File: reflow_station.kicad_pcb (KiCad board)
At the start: 2 copper layers, 6.5 x 0.7 mm, 252 parts, among them IC1 AMC23C10DWVR, IC2 MP100LGN-Z, J1 1731734, J10 DG301-5.0-02P-12-00A_H_, J11 USB_A, J12 USB_C_Receptacle_USB2.0_16P, J13 Conn_ARM_JTAG_SWD_10, J2 1707027, J3 1707027, J4 F52Q-1A7H1-11015, J5 1707027, J6 1707027, J7 DG301-5.0-02P-12-00A_H_, J8 DG301-5.0-02P-12-00A_H_, J9 DG301-5.0-02P-12-00A_H_, M1 Fan_CPU_4pin, M2 Fan_CPU_4pin, M3 Fan_CPU_4pin, M4 Fan_CPU_4pin, Q1 BTA16-600B, Q2 BTA16-600B, Q3 BTA16-600B, Q4 BTA16-600B, Q5 KSC1815YTA, SW2 SW_DIP_x08, SW3 SW_SPST, SW4 SW_SPST, SW5 SW_SPST, SW6 SW_Push, SW7 SW_SPDT, SW8 SW_SPDT, U1 TPS82130, U10 TPS2051BDBVR, U11 RCLAMP0504F.TCT, U12 STM32F469VITx, U13 RCLAMP0504F.TCT, U14 RCLAMP0504F.TCT, U2 RAC20-12SK, U3 MOC3023M, U4 MOC3023M, U5 TPS82130, U6 MOC3023M, U7 MOC3023M, U8 ADS1118IDGS, U9 ADS1118IDGS, Y1 25MHz, Y2 32.768kHz

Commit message: feat: populate elements on board
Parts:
- C1: footprint reflow_station_library:C_Axial_L12.0mm_D6.5mm_P15.00mm_Horizontal -> reflow_station_library:R474N31005001K
- R3: footprint reflow_station_library:R_0805_2012Metric_Pad1.20x1.40mm_HandSolder -> reflow_station_library:R_0402_1005Metric
- moved D5 132.4 mm to (78.6, 37.2)
- moved D2 130.2 mm to (78.6, 39.0)
- moved D1 128.1 mm to (78.6, 41.0)
- moved R3 118.7 mm to (90.9, 46.2), turned to 90 degrees
- moved C10 108.7 mm to (118.2, 129.3), turned to 90 degrees
- moved C15 108.3 mm to (97.0, 41.8)
- moved R27 104.5 mm to (81.5, 37.3)
- moved C11 103.7 mm to (116.2, 129.3)
- moved J1 101.6 mm to (79.1, 128.4)
- moved C16 100.2 mm to (111.8, 120.5), turned to 90 degrees
- moved C6 100.2 mm to (117.6, 114.9), turned to 180 degrees
- moved C20 99.2 mm to (115.1, 119.9), turned to -90 degrees
- moved R32 97.5 mm to (100.0, 39.9), turned to -90 degrees
- moved R31 97.5 mm to (100.0, 37.9), turned to -90 degrees
- moved R2 97.3 mm to (81.3, 39.1)
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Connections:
- D4 pad 2: /N -> GND1
- D4 pad 4: GND1 -> /N
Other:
- board size 6.5 x 0.7 mm -> 150 x 100 mm
- copper layers 2 -> 6

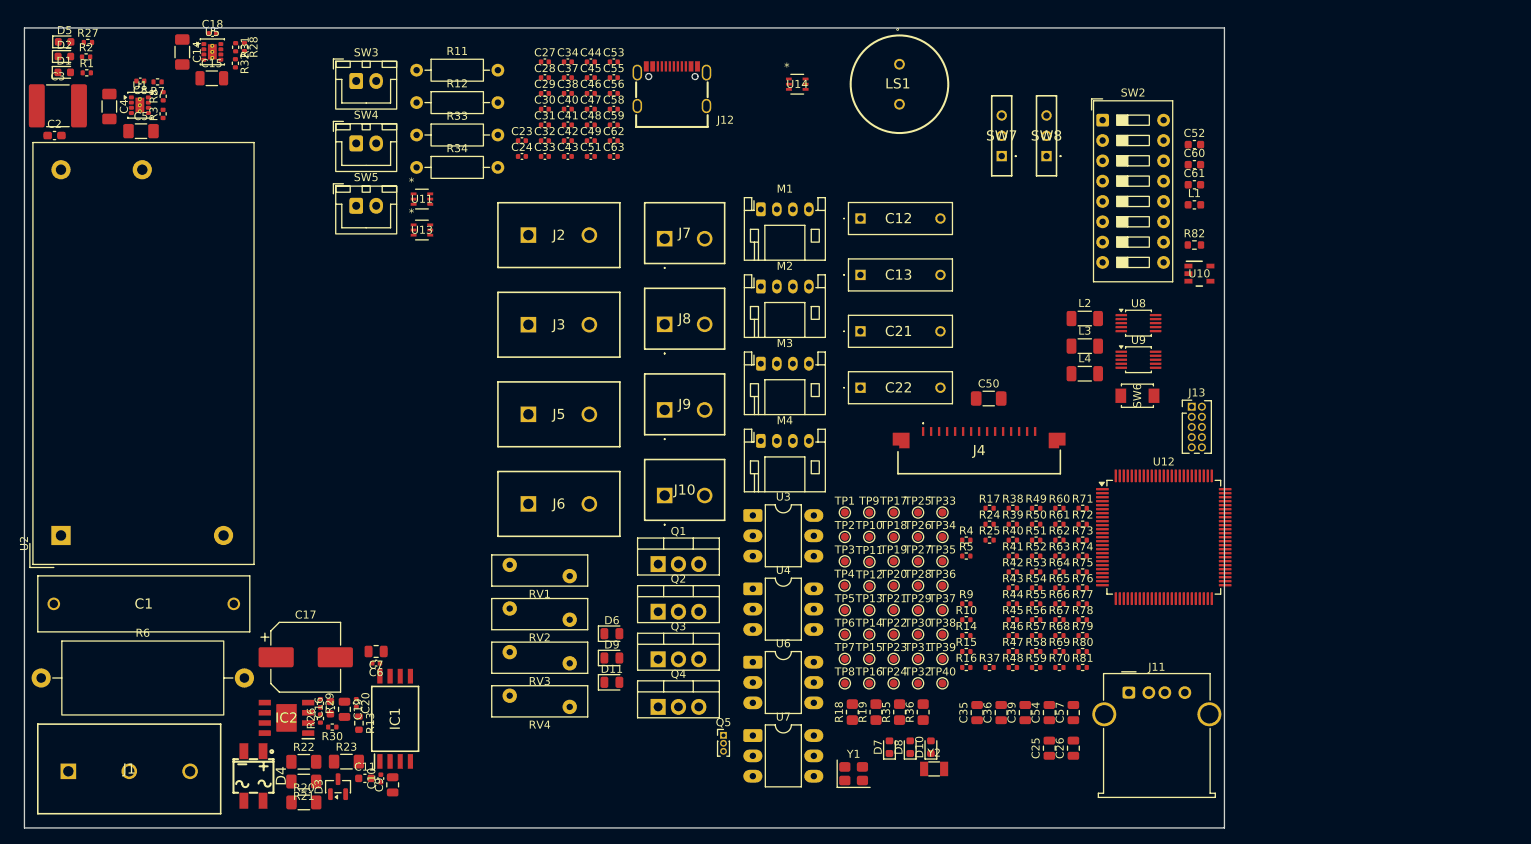
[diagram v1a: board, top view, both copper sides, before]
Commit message: feat: resize board; position elements more accurately; add mounting holes
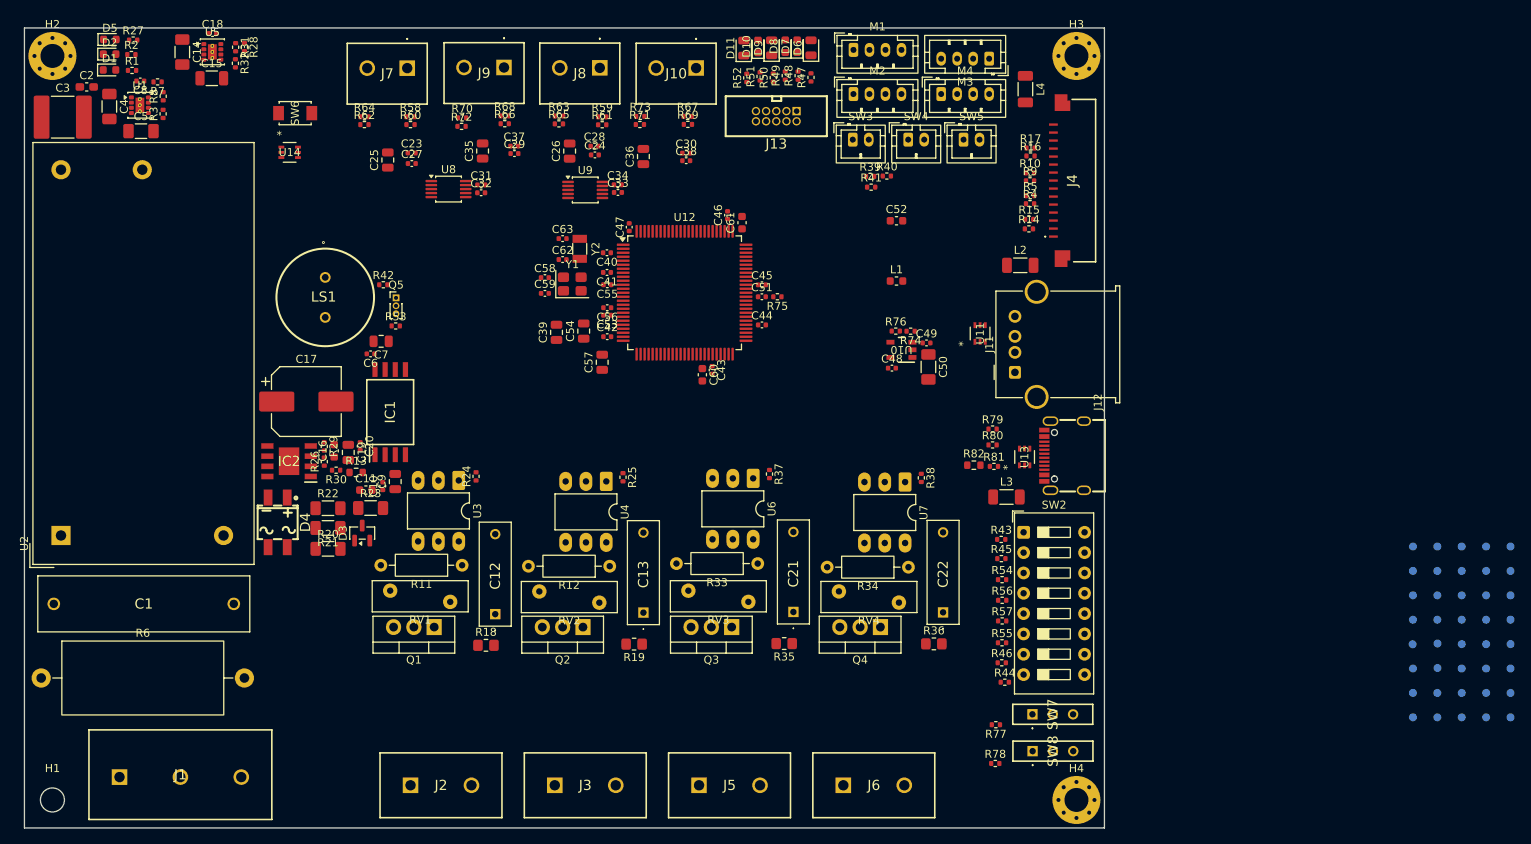
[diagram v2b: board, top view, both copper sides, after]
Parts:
- added H1: MountingHole_Pad, MountingHole:MountingHole_3mm, F.Cu at (77.1, 132.0)
- added H2: MountingHole_Pad, MountingHole:MountingHole_3mm_Pad_Via, F.Cu at (77.1, 39.0)
- added H3: MountingHole_Pad, MountingHole:MountingHole_3mm_Pad_Via, F.Cu at (205.1, 39.0)
- added H4: MountingHole_Pad, MountingHole:MountingHole_3mm_Pad_Via, F.Cu at (205.1, 132.0)
- J13: footprint reflow_station_library:PinHeader_2x05_P1.27mm_Vertical -> reflow_station_library:CONN-TH_10P-P1.27_HX-JN1.27-2X5P-ZZ-H4.9
- M1, M2, M3, M4: footprint reflow_station_library:JST_PH_S4B-PH-K_1x04_P2.00mm_Horizontal -> Connector_JST:JST_PH_B4B-PH-K_1x04_P2.00mm_Vertical
- SW3, SW4, SW5: footprint reflow_station_library:JST_XH_B2B-XH-A_1x02_P2.50mm_Vertical -> Connector_JST:JST_PH_B2B-PH-K_1x02_P2.00mm_Vertical
- TP1, TP10, TP11, TP12, TP13, TP14, TP15, TP16, TP17, TP18, TP19, TP2, TP20, TP21, TP22, TP23, TP24, TP25, TP26, TP27, TP28, TP29, TP3, TP30, TP31, TP32, TP33, TP34, TP35, TP36, TP37, TP38, TP39, TP4, TP40, TP5, TP6, TP7, TP8, TP9: moved to B.Cu
- moved SW6 111.0 mm to (107.5, 46.1)
- moved C25 110.6 mm to (119.0, 52.0)
- moved R64 103.8 mm to (116.1, 46.6)
- moved R58 102.9 mm to (121.8, 46.6)
- moved R70 101.5 mm to (128.3, 46.7)
- moved R62 101.2 mm to (116.1, 47.6)
- moved C26 97.7 mm to (141.8, 50.9)
- moved R68 95.0 mm to (133.7, 46.5)
- moved R60 94.2 mm to (121.9, 47.6)
- moved C35 93.5 mm to (130.9, 50.9)
- moved R72 92.2 mm to (128.2, 47.8)
- moved R66 91.7 mm to (133.7, 47.5)
- moved D10 90.2 mm to (165.3, 37.8)
- moved D8 89.0 mm to (168.7, 37.8)
- moved D7 88.4 mm to (170.2, 37.8)
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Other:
- board size 150 x 100 mm -> 135 x 100 mm

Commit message: feat: update library; change 2P connector for heaters
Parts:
- H1: footprint MountingHole:MountingHole_3mm -> reflow_station_library:MountingHole_3mm
- H2, H3, H4: footprint MountingHole:MountingHole_3mm_Pad_Via -> reflow_station_library:MountingHole_3mm_Pad_Via
- J2, J3, J5, J6: footprint reflow_station_library:1707027 -> reflow_station_library:1731721
- M1, M2, M3, M4: footprint Connector_JST:JST_PH_B4B-PH-K_1x04_P2.00mm_Vertical -> reflow_station_library:JST_PH_B4B-PH-K_1x04_P2.00mm_Vertical
- SW3, SW4, SW5: footprint Connector_JST:JST_PH_B2B-PH-K_1x02_P2.00mm_Vertical -> reflow_station_library:JST_PH_B2B-PH-K_1x02_P2.00mm_Vertical
- moved J6 2.30 mm to (173.7, 130.1)
- moved J5 1.54 mm to (156.4, 130.1)
- moved J3 0.79 mm to (139.1, 130.1)
- moved J2 0.10 mm to (121.8, 130.1)

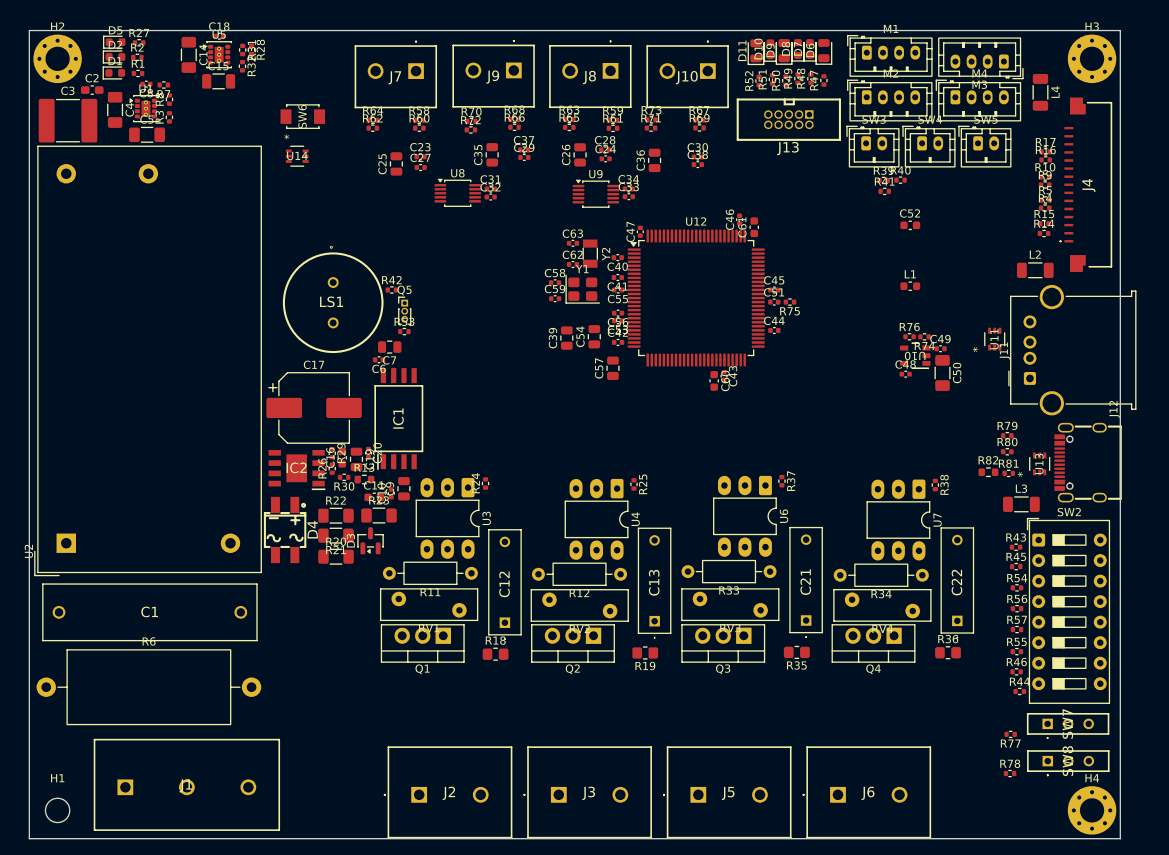
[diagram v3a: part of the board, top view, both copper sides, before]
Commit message: feat: add proper triac footprint with creepage drill
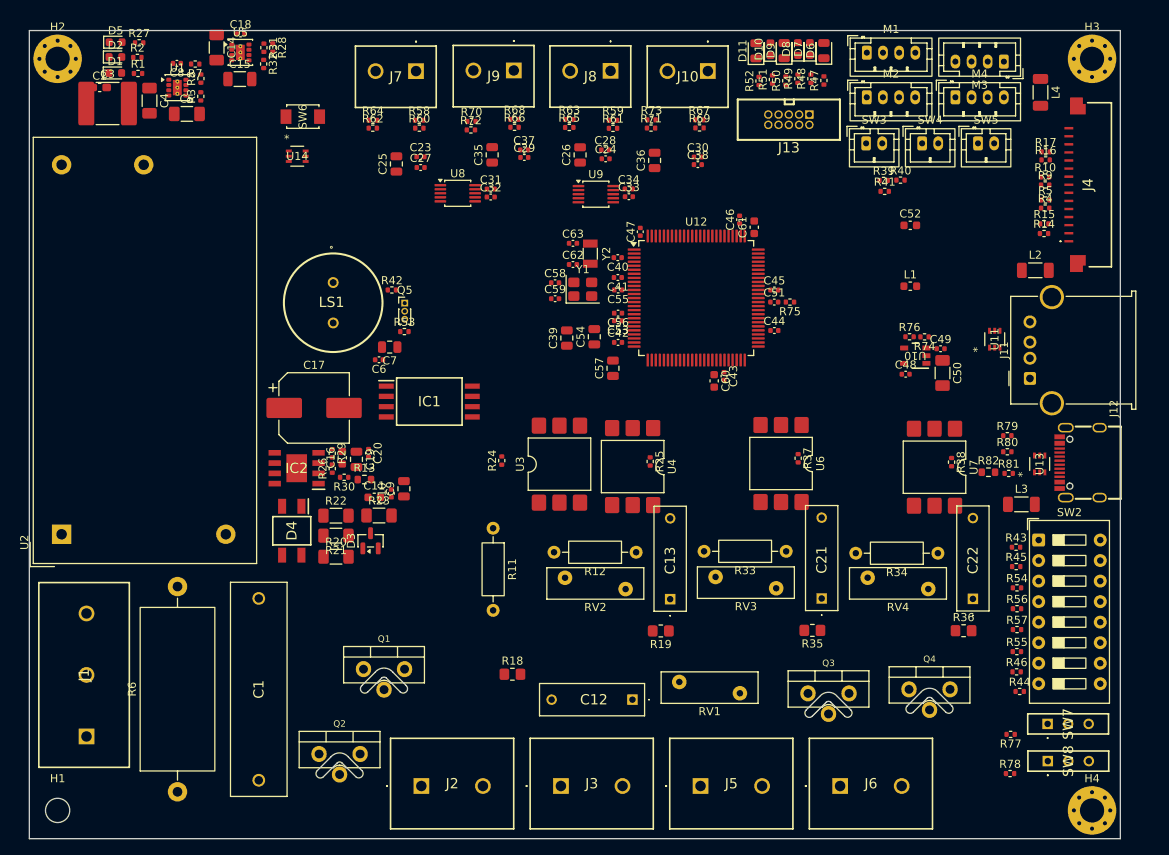
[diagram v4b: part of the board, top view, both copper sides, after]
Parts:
- D4: footprint reflow_station_library:MBS_L4.7-W3.8-P2.40-LS7.0-TL -> reflow_station_library:SOP240P700X300-4N
- Q1, Q2, Q3, Q4: footprint reflow_station_library:TO-220-3_Vertical -> reflow_station_library:TO-220-3_Vertical_Staggered
- R11, R12, R33, R34: value 330 1W fusible -> 470 1W fusible
- U3, U4, U6, U7: value MOC3023M -> MOC3052M; footprint reflow_station_library:DIP-6_W7.62mm_LongPads -> reflow_station_library:SMDIP-6_W9.53mm
- moved RV1 36.2 mm to (154.0, 116.1)
- moved Q2 34.7 mm to (112.0, 125.0), turned to 0 degrees
- moved C1 20.9 mm to (102.0, 128.2), turned to 90 degrees
- moved R6 20.8 mm to (91.9, 129.7), turned to 90 degrees
- moved C12 18.4 mm to (148.2, 118.3), turned to 180 degrees
- moved Q3 12.7 mm to (172.5, 117.5), turned to 0 degrees
- moved U3 11.7 mm to (139.2, 89.1), turned to 90 degrees
- moved Q1 8.41 mm to (117.5, 114.5), turned to 0 degrees
- moved Q4 7.95 mm to (185.0, 117.0), turned to 0 degrees
- moved J1 7.92 mm to (80.7, 122.8), turned to 90 degrees
- moved R11 6.19 mm to (131.0, 97.1), turned to -90 degrees
- moved C5 5.56 mm to (93.1, 45.8)
- moved C3 5.33 mm to (83.3, 44.5)
- moved R8 4.67 mm to (94.8, 41.4)
- moved R3 4.67 mm to (94.8, 43.6)
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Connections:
- Q1 pad 2: /L -> /L_FUSED
- Q2 pad 2: /L -> /L_FUSED
- Q3 pad 2: /L -> /L_FUSED
- Q4 pad 2: /L -> /L_FUSED
- R11 pad 2: /L -> /L_FUSED
- R12 pad 2: /L -> /L_FUSED
- R18 pad 1: /L -> /L_FUSED
- R19 pad 1: /L -> /L_FUSED
- R33 pad 2: /L -> /L_FUSED
- R34 pad 2: /L -> /L_FUSED
- R35 pad 1: /L -> /L_FUSED
- R36 pad 1: /L -> /L_FUSED
- RV1 pad 1: /L -> /L_FUSED
- RV2 pad 1: /L -> /L_FUSED
- RV3 pad 1: /L -> /L_FUSED
- RV4 pad 1: /L -> /L_FUSED

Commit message: feat: route high voltage traces
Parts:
- added HS1: Heatsink, Heatsink:Heatsink_Stonecold_HS-132_32x14mm_2xFixation1.5mm, F.Cu at (88.5, 115.5)
- added HS2: Heatsink, Heatsink:Heatsink_Stonecold_HS-132_32x14mm_2xFixation1.5mm, F.Cu at (122.5, 115.5)
- added HS3: Heatsink, Heatsink:Heatsink_Stonecold_HS-132_32x14mm_2xFixation1.5mm, F.Cu at (156.5, 115.5)
- added HS4: Heatsink, Heatsink:Heatsink_Stonecold_HS-132_32x14mm_2xFixation1.5mm, F.Cu at (190.5, 115.5)
- R18, R19, R35, R36: footprint reflow_station_library:R_0805_2012Metric_Pad1.20x1.40mm_HandSolder -> Capacitor_SMD:C_1210_3225Metric
- moved SW2 57.8 mm to (234.8, 53.5)
- moved R44 57.1 mm to (231.8, 72.7)
- moved R57 57.1 mm to (231.5, 65.0)
- moved R77 57.1 mm to (230.7, 78.0)
- moved R45 57.1 mm to (231.4, 57.2)
- moved R54 57.1 mm to (231.5, 59.8)
- moved R56 57.1 mm to (231.5, 62.4)
- moved R78 57.1 mm to (230.6, 82.8)
- moved SW7 57.1 mm to (235.3, 76.7)
- moved SW8 57.1 mm to (235.3, 81.3)
- moved R43 57.1 mm to (231.4, 54.8)
- moved R46 57.1 mm to (231.4, 70.2)
- moved R55 57.1 mm to (231.5, 67.7)
- moved C12 52.0 mm to (104.1, 90.7), turned to -90 degrees
- moved U3 48.7 mm to (90.5, 89.0), turned to -90 degrees
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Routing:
- net /L_FUSED: track 0.00 -> 295.8 mm
- net /N: track 0.00 -> 197.6 mm
- net Net-(Q1-A1): track 0.00 -> 46.6 mm
- net Net-(Q4-A1): track 0.00 -> 43.9 mm
- net Net-(Q2-A1): track 0.00 -> 43.9 mm
- net Net-(Q3-A1): track 0.00 -> 43.4 mm
- net Net-(C1-Pad1): track 0.00 -> 28.1 mm, vias 0 -> 1
- net Net-(Q1-G): track 0.00 -> 24.1 mm, vias 0 -> 1
- net Net-(Q4-G): track 0.00 -> 23.9 mm, vias 0 -> 1
- net Net-(Q3-G): track 0.00 -> 23.7 mm, vias 0 -> 1
- net Net-(Q2-G): track 0.00 -> 23.1 mm, vias 0 -> 1
- net Net-(C22-Pad1): track 0.00 -> 9.20 mm
- net Net-(C12-Pad1): track 0.00 -> 9.18 mm
- net Net-(C13-Pad1): track 0.00 -> 9.17 mm
- net Net-(C21-Pad1): track 0.00 -> 9.17 mm
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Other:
- board size 135 x 100 mm -> 170 x 100 mm

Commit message: feat: write down whole BOM
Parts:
- C2: value 100n 25V -> 100n; footprint reflow_station_library:C_0603_1608Metric_Pad1.08x0.95mm_HandSolder -> reflow_station_library:C_0402_1005Metric
- C3: value 47u 25V -> 47u
- HS1, HS2, HS3, HS4: footprint Heatsink:Heatsink_Stonecold_HS-132_32x14mm_2xFixation1.5mm -> reflow_station_library:Heatsink_Stonecold_HS-132_32x14mm_2xFixation1.5mm
- L1: value FCM1608KF-601T03 -> 600R @ 100MHz
- Q5: footprint reflow_station_library:PinHeader_1x03_P1.00mm_Vertical -> reflow_station_library:TO-92L_Inline_Wide
- R11, R12, R33, R34: footprint reflow_station_library:R_Axial_DIN0207_L6.3mm_D2.5mm_P10.16mm_Horizontal -> reflow_station_library:R_Axial_DIN0411_L9.9mm_D3.6mm_P15.24mm_Horizontal
- R18, R19, R35, R36: footprint Capacitor_SMD:C_1210_3225Metric -> reflow_station_library:C_1210_3225Metric
- R20, R21, R22: value 1.09M 1% -> 1.09M
- R29: value 90.9k 1% -> 90.9k
- R30: value 10.2k 1% -> 10.2k
- R6: footprint reflow_station_library:R_Axial_DIN0922_L20.0mm_D9.0mm_P25.40mm_Horizontal -> reflow_station_library:R_Axial_DIN0516_L15.5mm_D5.0mm_P20.32mm_Horizontal
- U12: value STM32F469VITx -> STM32F469VIT6
- moved SW2 71.9 mm to (164.5, 38.5)
- moved R44 71.1 mm to (162.6, 56.4), turned to 90 degrees
- moved R55 70.8 mm to (162.6, 51.4), turned to 90 degrees
- moved R57 70.7 mm to (162.6, 48.9), turned to 90 degrees
- moved R46 70.7 mm to (162.6, 53.9), turned to 90 degrees
- moved R56 70.7 mm to (162.6, 46.3), turned to 90 degrees
- moved R54 70.7 mm to (162.6, 43.8), turned to 90 degrees
- moved R43 70.6 mm to (162.6, 38.7), turned to 90 degrees
- moved R45 70.6 mm to (162.6, 41.3), turned to 90 degrees
- moved SW7 66.3 mm to (170.7, 61.7)
- moved SW8 66.3 mm to (170.7, 66.3)
- moved R77 66.3 mm to (166.1, 63.0)
- moved R78 66.3 mm to (166.0, 67.8)
- moved C6 17.5 mm to (98.4, 72.4), turned to 90 degrees
- moved C9 16.6 mm to (86.6, 69.5), turned to 180 degrees
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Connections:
- H3 pad 1: /SHIELD -> Earth
- H4 pad 1: /SHIELD -> Earth
- J11 pad SH: /SHIELD -> Earth
- J12 pad SH: /SHIELD -> Earth
- J13 pad 9: /SHIELD -> Earth
- J4 pad MP1: /SHIELD -> Earth
- J4 pad MP2: /SHIELD -> Earth
- J4 pad MP3: /SHIELD -> Earth
- J4 pad MP4: /SHIELD -> Earth
- L2 pad 2: /SHIELD -> Earth
- L3 pad 2: /SHIELD -> Earth
- L4 pad 2: /SHIELD -> Earth
- U11 pad 2: /SHIELD -> Earth
- U13 pad 2: /SHIELD -> Earth
- U14 pad 2: /SHIELD -> Earth
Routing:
- net /L_FUSED: track 295.8 -> 317.4 mm
- net Net-(D3-COM): track 0.00 -> 14.3 mm
- net /L_RECTIFIED: track 0.00 -> 14.0 mm
- net /N: track 197.6 -> 210.6 mm
- net GND1: track 0.00 -> 8.15 mm
- net Net-(IC2-VB): track 0.00 -> 6.14 mm
- net Net-(IC2-PG): track 0.00 -> 5.81 mm
- net Net-(C1-Pad1): track 28.1 -> 23.1 mm
- net Net-(IC1-INP): track 0.00 -> 4.08 mm
- net Net-(IC2-FB): track 0.00 -> 3.91 mm
- net Net-(R21-Pad2): track 0.00 -> 1.84 mm
- net Net-(R20-Pad2): track 0.00 -> 1.81 mm
- net /+12V_ISOLATED: track 0.00 -> 1.69 mm
- added copper zone on In1.Cu, net Earth
- added copper zone on In1.Cu, net GND
- added copper zone on In1.Cu, net GND1
